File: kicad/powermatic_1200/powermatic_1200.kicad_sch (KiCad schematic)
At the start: 62 parts, among them J1 T4171310004-001, J2 3PH-4W-PLUG, J3 BNSPDX-23-W, J4 BSPDX-23-W, J5 BSPBX-22-W, K1 HMC-9B30-11-DS, K2 HMC-9B30-11-DS, K3 HC3096N-52-900-24, K4 HMC-9B30-11-DS, K5 HMC-9B30-11-DS, K6 HMC-9B30-11-DS, M1 PWRM1200-MOTOR, Q1 FAZ-D4/2-NA-L, SW1 222102

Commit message: massage schematic for understanding
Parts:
- removed J3: BNSPDX-23-W, Controls:BNSPDX-23-W_BottomWall, symbol Controls:BNSPDX-23-W
- removed J5: BSPBX-22-W, Controls:BSPBX-22-W_BottomWall, symbol Controls:BSPBX-22-W
- removed S2: 800 Type 3SA, symbol non_lcsc_parts:Non-LCSC/800S-3SA
- removed S3: 365-TAV2111, symbol non_lcsc_parts:Non-LCSC/365-TAV2111
- removed TB22, TB23: KN-T12GRY-25, Controls:KN-T12GRY-25_Front, symbol Controls:KN-T12GRY-25
- added J3: BSPBX-22-W, Controls:BSPBX-22-W_BottomWall, symbol non_lcsc_parts:Non-LCSC/BSPBX-22-W
- added J7: BNSPDX-23-W, Controls:BNSPDX-23-W_BottomWall, symbol Controls:BNSPDX-23-W
- added S2: 800 Type 3SA, symbol Controls:800S-3SA
- added S3: 365-TAV2111, symbol Controls:365-TAV2111
- added TB4, TB5, TB6, TB7, TB8: KN-T12GRY-25, Controls:KN-T12GRY-25_Front, symbol Controls:KN-T12GRY-25
- added TB53: KN-G12SP-10, Controls:KN-G12SP-10_Front, symbol Controls:KN-G12SP-10
- J2: Part Name Power Plug -> Mains Plug
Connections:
- net FWD_CMD: now also J3.5, S2.R1 (FWD_NO_2), TB6.BOT (TERM), TB6.TOP (TERM)
- net HIGH_CMD: now also J3.3, S3.2.U (HI2_U), TB5.BOT (TERM), TB5.TOP (TERM)
- net L1_IN: now also J7.X (L1)
- net L2_IN: now also J7.Y (L2)
- net L3_IN: now also J7.Z (L3)
- net LOW_CMD: now also J3.2, S3.1.U (LOW1_U), S3.3.U (HI3_U), TB4.BOT (TERM), TB4.TOP (TERM)
- net M1_T1: no longer TB61.BOT (TERM)
- net M1_T2: no longer TB63.BOT (TERM)
- net M1_T3: no longer TB65.BOT (TERM)
- net M1_T4: now also J4.T6, M1.T6, OL2.2 (T1), TB68.BOT (TERM), TB68.TOP (TERM); no longer J4.T4, M1.T4, OL2.4 (T2), TB66.BOT (TERM), TB66.TOP (TERM)
- net M1_T5: now also J4.T4, M1.T4, OL2.4 (T2), TB66.BOT (TERM), TB66.TOP (TERM); no longer J4.T5, M1.T5, OL2.6 (T3), TB67.BOT (TERM), TB67.TOP (TERM)
- net M1_T6: now also J4.T5, M1.T5, OL2.6 (T3), TB67.BOT (TERM), TB67.TOP (TERM); no longer J4.T6, M1.T6, OL2.2 (T1), TB68.BOT (TERM), TB68.TOP (TERM)
- net PE: now also J7.G (GND), TB53.BOT (TERM), TB53.PE, TB53.TOP (TERM)
- net REV_CMD: now also J3.6, S2.R3 (REV_NO_2), TB7.BOT (TERM), TB7.TOP (TERM)
- net ESTOP_JUMPER: now reaches J1.2, J1.3, J6.2, J6.3, S1.2 (NC2/WHI), S1.3 (NC1/BLK), TB31.BOT (TERM), TB31.TOP (TERM), TB32.BOT (TERM), TB32.TOP (TERM)
- net +24V_CTRL renamed STOP_RELEASED
- net STOP_RELEASED: now also J3.1, J3.7 (8), S2.L5 (STOP_NC_1), S3.1.L (LOW1_L), S3.2.L (HI2_L)
- net +24V_RUN renamed SPEED_SET
- net SPEED_SET: now also J3.4, S2.L2 (FWD_NO_1), S2.L4 (REV_NO_1)
- net STOP_CHAIN renamed OVERLOAD_OK
- net OVERLOAD_OK: now also J3.7 (8), S2.R5 (STOP_NC_2), TB8.BOT (TERM), TB8.TOP (TERM)
- new net: S3.3.L (HI3_L), S3.4.L (LOW4_L), S3.5.L (HI5_L)
- new net: S3.4.U (LOW4_U), S3.6.U (HI6_U)
- new net: S3.5.U (HI5_U), S3.7.U (LOW7_U)
- new net: S3.7.L (LOW7_L), S3.8.L (HI8_L)
- new net: S2.R2 (FWD_NC_2), S2.R4 (REV_NC_2)
- no-connect marks 20 -> 23
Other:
- note added: "DIN_BOT"
- note added: "DIN_TOP"
- note added: "J2.GND"
- note removed: "J2.G"
- note removed: "J5.1"
- note removed: "J5.2"
- note removed: "K1.43"
- note removed: "K2.43"
- note removed: "K4.43"
- note removed: "K4.44"
- note removed: "K5.2"
- note removed: "K5.4"
- note removed: "K5.6"
- note removed: "K6.43"
- note removed: "K6.44"
- note removed: "M1.T1"
- note removed: "M1.T2"
- note removed: "M1.T3"
- note removed: "M1.T4"
- note removed: "M1.T5"
- note removed: "M1.T6"
- note removed: "OL1A.2"
- note removed: "OL1A.4"
- note removed: "OL1A.6"
- note removed: "OL2A.2"
- note removed: "OL2A.4"
- note removed: "OL2A.6"
- note removed: "PS1.TB1.1"
- moved on the sheet: FH1, J1, J2, J4, J6, K1A, K2B, K4A, K4B, K5A, K5B, K6A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

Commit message: Integrate vintage controls and standardize panel artwork
Update the schematic, PCB, BOM and wiring-size/termination tools for the control-station and conduit plans. Preserve physical terminal mappings and detailed Fab artwork while reserving user layers for enclosure information. Include KiCad migration and review checkpoints; native DRC remains unverified after checker crashes.
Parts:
- removed J3: BSPBX-22-W, Controls:BSPBX-22-W_BottomWall, symbol non_lcsc_parts:Non-LCSC/BSPBX-22-W
- removed J4: BSPDX-23-W, Controls:BSPDX-23-W_BottomWall, symbol Controls:BSPDX-23-W
- removed J7: BNSPDX-23-W, Controls:BNSPDX-23-W_BottomWall, symbol Controls:BNSPDX-23-W
- removed K1, K2, K4, K5, K6: HMC-9B30-11-DS, Controls:HMC-9B30-11-DS_Front, symbol non_lcsc_parts:Non-LCSC/HMC-9B30-11-DS
- removed MI1, MI2: HMX1-MI, Controls:HMX1-MI_Front, symbol non_lcsc_parts:Non-LCSC/HMX1-MI
- removed OL1, OL2: HTOR32-6-S, Controls:HTOR32-6-S_Front, symbol non_lcsc_parts:Non-LCSC/HTOR32-6-S
- removed SP3: HMX1-SSVRC-DC, Controls:HMX1-SSVRC-DC_Front, symbol non_lcsc_parts:Non-LCSC/HMX1-SSVRC-DC
- removed TB1, TB10, TB11, TB12, TB13, TB14, TB2, TB20, TB21, TB24, TB3, TB30, TB31, TB32, TB33, TB4, TB40, TB41, TB42, TB5, TB6, TB60, TB61, TB62, TB63, TB64, TB65, TB66, TB67, TB68, TB7, TB8: KN-T12GRY-25, Controls:KN-T12GRY-25_Front, symbol Controls:KN-T12GRY-25
- removed TB50, TB51, TB52, TB53: KN-G12SP-10, Controls:KN-G12SP-10_Front, symbol Controls:KN-G12SP-10
- added K1, K2, K4, K5, K6: HMC-9B30-11-DS, Controls:HMC-9B30-11-DS_Front, symbol Controls:HMC-9B30-11-DS
- added OL4, OL6: HTOR32-6-S, Controls:HTOR32-6-S_Front, symbol Controls:HTOR32-6-S
- added SP6: HMX1-SSVRC-DC, Controls:HMX1-SSVRC-DC_Front, symbol non_lcsc_parts:Non-LCSC/HMX1-SSVRC-DC
- FH1: Mounting (none) -> din_top; Part Name Class R Fuse Holder -> Fuse Holder; Termination.P1.A (none) -> Ferrule 14 AWG; L=TBD mm; Termination.P1.B (none) -> Ferrule 14 AWG; L=TBD mm; Termination.P2.A (none) -> Ferrule 14 AWG; L=TBD mm; Termination.P2.B (none) -> Ferrule 14 AWG; L=TBD mm; Termination.P3.A (none) -> Ferrule 14 AWG; L=TBD mm; Termination.P3.B (none) -> Ferrule 14 AWG; L=TBD mm; Wire.Sizes (none) -> {"schema":1,"owner_uuid":"5ca8057b-4eb2-4c19-b9e6-24988ef26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; WireName Fuse Holder -> (none)
- H1: Mounting (none) -> panel; Termination.X1 (none) -> Ferrule 18 AWG; L=TBD mm; Termination.X2 (none) -> Ferrule 18 AWG; L=TBD mm; Wire.Sizes (none) -> {"schema":1,"owner_uuid":"a7bde42c-14f2-46ec-a0af-e6c2b915b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
- J1: Mounting (none) -> panel; Termination.1 (none) -> Factory pigtail, 22 AWG (retained); Termination.2 (none) -> Factory pigtail, 22 AWG (retained); Termination.3 (none) -> Factory pigtail, 22 AWG (retained); Termination.4 (none) -> Factory pigtail, 22 AWG (retained); Wire.Sizes (none) -> {"schema":1,"owner_uuid":"b4d1b4ae-f9ca-4a9a-a340-a64e26a69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
- J2: Mounting (none) -> machine; Termination.G (none) -> Plug clamp, 12 AWG; Termination.X (none) -> Plug clamp, 12 AWG; Termination.Y (none) -> Plug clamp, 12 AWG; Termination.Z (none) -> Plug clamp, 12 AWG; Wire.Sizes (none) -> {"schema":1,"owner_uuid":"c5ff8006-339f-4474-94f3-df6cc7c1d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; WireName Mains Plug -> (none)
- J6: value ~ -> (none); Mounting (none) -> machine; Termination.1 (none) -> M12 mating contact (retained); Termination.2 (none) -> M12 mating contact (retained); Termination.3 (none) -> M12 mating contact (retained); Termination.4 (none) -> M12 mating contact (retained); Wire.Sizes (none) -> {"schema":1,"owner_uuid":"b5200e46-0e22-4b8b-8db6-9eae3d708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
- K3: Mounting (none) -> din_bot; Termination.13 (none) -> Ferrule 18 AWG; L=TBD mm; Termination.14 (none) -> Ferrule 18 AWG; L=TBD mm; Termination.23 (none) -> Ferrule 18 AWG; L=TBD mm; Termination.24 (none) -> Ferrule 18 AWG; L=TBD mm; Termination.31 (none) -> N/A — unused pin; Termination.32 (none) -> N/A — unused pin; Termination.41 (none) -> N/A — unused pin; Termination.42 (none) -> N/A — unused pin; Termination.A1+ (none) -> Ferrule 18 AWG; L=TBD mm; Termination.A2 (none) -> Ferrule 18 AWG; L=TBD mm; Wire.Sizes (none) -> {"schema":1,"owner_uuid":"40692fa1-1db0-4fd6-bab3-8a72882b1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
- M1: Mounting (none) -> machine; Termination.PE (none) -> Wire-splice connector, 12 AWG; Termination.T1 (none) -> Wire-splice connector, 14 AWG; Termination.T2 (none) -> Wire-splice connector, 14 AWG; Termination.T3 (none) -> Wire-splice connector, 14 AWG; Termination.T4 (none) -> Wire-splice connector, 14 AWG; Termination.T5 (none) -> Wire-splice connector, 14 AWG; Termination.T6 (none) -> Wire-splice connector, 14 AWG; Wire.SizePlan (none) -> {"schema":1,"owner_uuid":"f758497e-4710-4fd6-9851-f0e206557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; Wire.Sizes (none) -> {"schema":1,"owner_uuid":"f758497e-4710-4fd6-9851-f0e206557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
- PS1: JLCPCB Assembly Unknown -> (none); JLCPCB Checked UTC 2026-09-23T00:57:12+00:00 -> (none); JLCPCB Class Unmapped -> (none); JLCPCB Match No exact MPN in returned results -> (none); JLCPCB Source https://jlcpcb.com/parts/componentSearch?searchTxt=NDR-240-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 -> (none); Mounting (none) -> din_bot; Termination.1_BOT (none) -> Ferrule 14 AWG; L=TBD mm; Termination.1_TOP (none) -> Ferrule 18 AWG; L=TBD mm; Termination.2_BOT (none) -> Ferrule 14 AWG; L=TBD mm; Termination.2_TOP (none) -> Ferrule 18 AWG; L=TBD mm; Termination.3_BOT (none) -> Ferrule 14 AWG; L=TBD mm; Termination.3_TOP (none) -> Ferrule 18 AWG; L=TBD mm; Termination.4_TOP (none) -> Ferrule 18 AWG; L=TBD mm; Wire.SizePlan (none) -> {"schema":1,"owner_uuid":"b71e1787-97a1-40f8-b061-785c34849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; Wire.Sizes (none) -> {"schema":1,"owner_uuid":"b71e1787-97a1-40f8-b061-785c34849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
- Q1: Mounting (none) -> din_bot; Termination.1 (none) -> Ferrule 14 AWG; L=TBD mm; Termination.2 (none) -> Ferrule 14 AWG; L=TBD mm; Termination.3 (none) -> Ferrule 14 AWG; L=TBD mm; Termination.4 (none) -> Ferrule 14 AWG; L=TBD mm; Wire.Sizes (none) -> {"schema":1,"owner_uuid":"b75c22a6-5008-468e-8688-fb1a0cea0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
- S1: Mounting (none) -> machine; Termination.1 (none) -> Supplied assembly connection (retained); Termination.2 (none) -> Supplied assembly connection (retained); Termination.3 (none) -> Supplied assembly connection (retained); Termination.4 (none) -> Supplied assembly connection (retained); Wire.Sizes (none) -> {"schema":1,"owner_uuid":"dbf6d1f8-0025-4137-ac1b-c2a9236e3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
- S2: value 800 Type 3SA -> 50MA3KLE; footprint (none) -> Controls:50MA3KLE_Top; symbol Controls:800S-3SA -> Controls:50MA3KLE; MPN (none) -> 50MA3KLE; Manufacturer Allen-Bradley -> Furnas; Mounting (none) -> machine; Package (none) -> Machine-mounted pushbutton station 52 x 116 x 44.7 mm; Termination.1B (none) -> Ring terminal, 16 AWG; stud=#8-32; OD<=9 mm; Termination.1T (none) -> Retained jumper; Termination.2B (none) -> Ring terminal, 16 AWG; stud=#8-32; OD<=9 mm; Termination.2T (none) -> N/A — unused pin; Termination.3B (none) -> Ring terminal, 16 AWG; stud=#8-32; OD<=9 mm; Termination.3T (none) -> Retained jumper; Termination.4B (none) -> Required jumper, 2B-4B; Termination.4T (none) -> N/A — unused pin; Termination.5T (none) -> Ring terminal, 16 AWG; stud=#8-32; OD<=9 mm; Termination.6T (none) -> Ring terminal, 16 AWG; stud=#8-32; OD<=9 mm; Wire.Sizes (none) -> {"schema":1,"owner_uuid":"9cff5cf5-fbfa-495e-9dc5-ac2f98a5c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
- S3: footprint (none) -> Controls:365-TAV2111_Top; Mounting (none) -> machine; Package (none) -> Machine-mounted drum switch 156 x 73 x 75 mm; Termination.1.L (none) -> Ring terminal, 16 AWG; stud=#8-32; OD<=9 mm; Termination.1.U (none) -> Ring terminal, 16 AWG; stud=#8-32; OD<=9 mm; Termination.2.L (none) -> Retained jumper; Termination.2.U (none) -> Ring terminal, 16 AWG; stud=#8-32; OD<=9 mm; Termination.3.L (none) -> Retained jumper; Termination.3.U (none) -> Retained jumper; Termination.4.L (none) -> Retained jumper; Termination.4.U (none) -> Retained jumper; Termination.5.L (none) -> Retained jumper; Termination.5.U (none) -> Retained jumper; Termination.6.L (none) -> N/A — unused pin; Termination.6.U (none) -> Retained jumper; Termination.7.L (none) -> Retained jumper; Termination.7.U (none) -> Retained jumper; Termination.8.L (none) -> Retained jumper; Termination.8.U (none) -> N/A — unused pin; Wire.Sizes (none) -> {"schema":1,"owner_uuid":"26502bde-0b19-4cea-bdff-2e8d228f3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
- SP1: Mounting (none) -> din_top; Termination.1 (none) -> Supplied fork-ended lead (retained); Termination.2 (none) -> Supplied fork-ended lead (retained); Wire.Sizes (none) -> {"schema":1,"owner_uuid":"c89c0a24-66e3-4ec6-9e05-4125689b4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
- SP2: Mounting (none) -> din_top; Termination.1 (none) -> Supplied fork-ended lead (retained); Termination.2 (none) -> Supplied fork-ended lead (retained); Wire.Sizes (none) -> {"schema":1,"owner_uuid":"cf360c79-7593-4c8a-bc81-2460b3d4c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
- SP4: Mounting (none) -> din_bot; Termination.1 (none) -> Supplied fork-ended lead (retained); Termination.2 (none) -> Supplied fork-ended lead (retained); Wire.Sizes (none) -> {"schema":1,"owner_uuid":"243d7eb4-7102-4a9f-94c3-46f62fdca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
- SP5: Mounting (none) -> din_bot; Termination.1 (none) -> Supplied fork-ended lead (retained); Termination.2 (none) -> Supplied fork-ended lead (retained); Wire.Sizes (none) -> {"schema":1,"owner_uuid":"8ee9f0e8-f022-4223-9694-e57327052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
- SW1: Mounting (none) -> panel; Termination.1 (none) -> Ferrule 14 AWG; L=TBD mm; Termination.2 (none) -> Ferrule 14 AWG; L=TBD mm; Termination.3 (none) -> Ferrule 14 AWG; L=TBD mm; Termination.4 (none) -> Ferrule 14 AWG; L=TBD mm; Termination.5 (none) -> Ferrule 14 AWG; L=TBD mm; Termination.6 (none) -> Ferrule 14 AWG; L=TBD mm; Wire.Sizes (none) -> {"schema":1,"owner_uuid":"de43fc54-ea53-4062-9d14-222047b23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
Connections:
- net +24V_EN: now also OL4.95 (TRIP_NC_1)
- net 0V: now also K1.A2.BOT (A2_BOT), K1.A2.TOP (A2_TOP), K2.A2.BOT (A2_BOT), K2.A2.TOP (A2_TOP), K4.A2.BOT (A2_BOT), K4.A2.TOP (A2_TOP), K5.A2.BOT (A2_BOT), K5.A2.TOP (A2_TOP), K6.A2.BOT (A2_BOT), K6.A2.TOP (A2_TOP), SP6.2 (SUP_2)
- net FWD_CMD: now also S2.1B (FWD_NO_1), K1.44 (AUX_NO_2), K2.31 (AUX_NC_1); no longer S2.R1 (FWD_NO_2)
- net HIGH_CMD: now also K4.31 (AUX_NC_1)
- net HS_SHORT: now also K5.1 (L1), K5.3 (L2), K5.5 (L3)
- net L1_DIR: now also K1.2 (T1), K2.6 (T3), K4.1 (L1), K6.1 (L1)
- net L1_SW: now also K1.1 (L1), K2.1 (L1)
- net L2_DIR: now also K1.4 (T2), K2.4 (T2), K4.3 (L2), K6.3 (L2)
- net L2_SW: now also K1.3 (L2), K2.3 (L2)
- net L3_DIR: now also K1.6 (T3), K2.2 (T1), K4.5 (L3), K6.5 (L3)
- net L3_SW: now also K1.5 (L3), K2.5 (L3)
- net LOW_CMD: now also K6.31 (AUX_NC_1)
- net M1_T1: now also K5.2 (T1), OL4.2 (T1)
- net M1_T2: now also K5.4 (T2), OL4.4 (T2)
- net M1_T3: now also K5.6 (T3), OL4.6 (T3)
- net M1_T4: now also M1.T4, OL6.2 (T1); no longer M1.T6
- net M1_T5: now also M1.T5, OL6.4 (T2); no longer M1.T4
- net M1_T6: now also M1.T6, OL6.6 (T3); no longer M1.T5
- net OVERLOAD_OK: now also S2.1T (FWD_NC_1), S2.3T (REV_NC_1), S2.5T (STOP_NC_1), OL6.96 (TRIP_NC_2); no longer S2.R5 (STOP_NC_2)
- net PE: now also M1.PE
- net REV_CMD: now also S2.3B (REV_NO_1), K1.31 (AUX_NC_1), K2.44 (AUX_NO_2); no longer S2.R3 (REV_NO_2)
- net SPEED_SET: now also S2.2B (FWD_NO_2), S2.4B (REV_NO_2), K1.43 (AUX_NO_1), K2.43 (AUX_NO_1), K4.44 (AUX_NO_2), K6.44 (AUX_NO_2); no longer S2.L2 (FWD_NO_1), S2.L4 (REV_NO_1)
- net STOP_RELEASED: now also S2.6T (STOP_NC_2), K4.43 (AUX_NO_1), K6.43 (AUX_NO_1); no longer S2.L5 (STOP_NC_1)
- net HS_COIL: now reaches SP5.1 (SUP_1)
- net HS_COIL: now also K4.32 (AUX_NC_2), K5.43 (AUX_NO_1), K5.A1.BOT (A1_BOT), K5.A1.TOP (A1_TOP)
- net FWD_COIL: now reaches SP1.1 (SUP_1)
- net FWD_COIL: now also K1.A1.BOT (A1_BOT), K1.A1.TOP (A1_TOP), K2.32 (AUX_NC_2)
- net REV_COIL: now reaches SP2.1 (SUP_1)
- net REV_COIL: now also K1.32 (AUX_NC_2), K2.A1.BOT (A1_BOT), K2.A1.TOP (A1_TOP)
- net K3_JUMPER: now reaches K3.14 (NO1), K3.23 (NO2)
- net LOW_COIL: now reaches SP4.1 (SUP_1)
- net LOW_COIL: now also K4.A1.BOT (A1_BOT), K4.A1.TOP (A1_TOP), K5.32 (AUX_NC_2)
- new net HIGH_COIL: K5.44 (AUX_NO_2), K6.A1.BOT (A1_BOT), K6.A1.TOP (A1_TOP), SP6.1 (SUP_1)
- new net L1_HIGH: K6.2 (T1), OL6.IN1 (L1)
- new net L1_LOW: K4.2 (T1), OL4.IN1 (L1)
- new net L2_HIGH: K6.4 (T2), OL6.IN2 (L2)
- new net L2_LOW: K4.4 (T2), OL4.IN2 (L2)
- new net L3_HIGH: K6.6 (T3), OL6.IN3 (L3)
- new net L3_LOW: K4.6 (T3), OL4.IN3 (L3)
- new net LOW_K6_OK: K5.31 (AUX_NC_1), K6.32 (AUX_NC_2)
- new net OL4_OK: OL4.96 (TRIP_NC_2), OL6.95 (TRIP_NC_1)
- no-connect marks 23 -> 12
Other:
- note removed: "3"
- note removed: "4"
- note removed: "5"
- note removed: "BACKPLATE"
- note removed: "DIN_BOT"
- note removed: "DIN_TOP"
- note removed: "DOOR"
- note removed: "H1.X1"
- note removed: "H1.X2"
- note removed: "J1.1"
- note removed: "J2.GND"
- note removed: "K1.A2_BOT"
- note removed: "K2.A2_BOT"
- note removed: "K3.13"
- note removed: "K3.A2"
- note removed: "K4.A2_BOT"
- note removed: "K5.A2_BOT"
- note removed: "K6.A2_BOT"
- note removed: "MOTOR"
- note removed: "PS1.TB2.1"
- note removed: "PS1.TB2.3"
- note removed: "SPARE"
- moved on the sheet: FH1, H1, J1, J2, J6, K3, PS1, Q1, S1, S2, S3, SW1

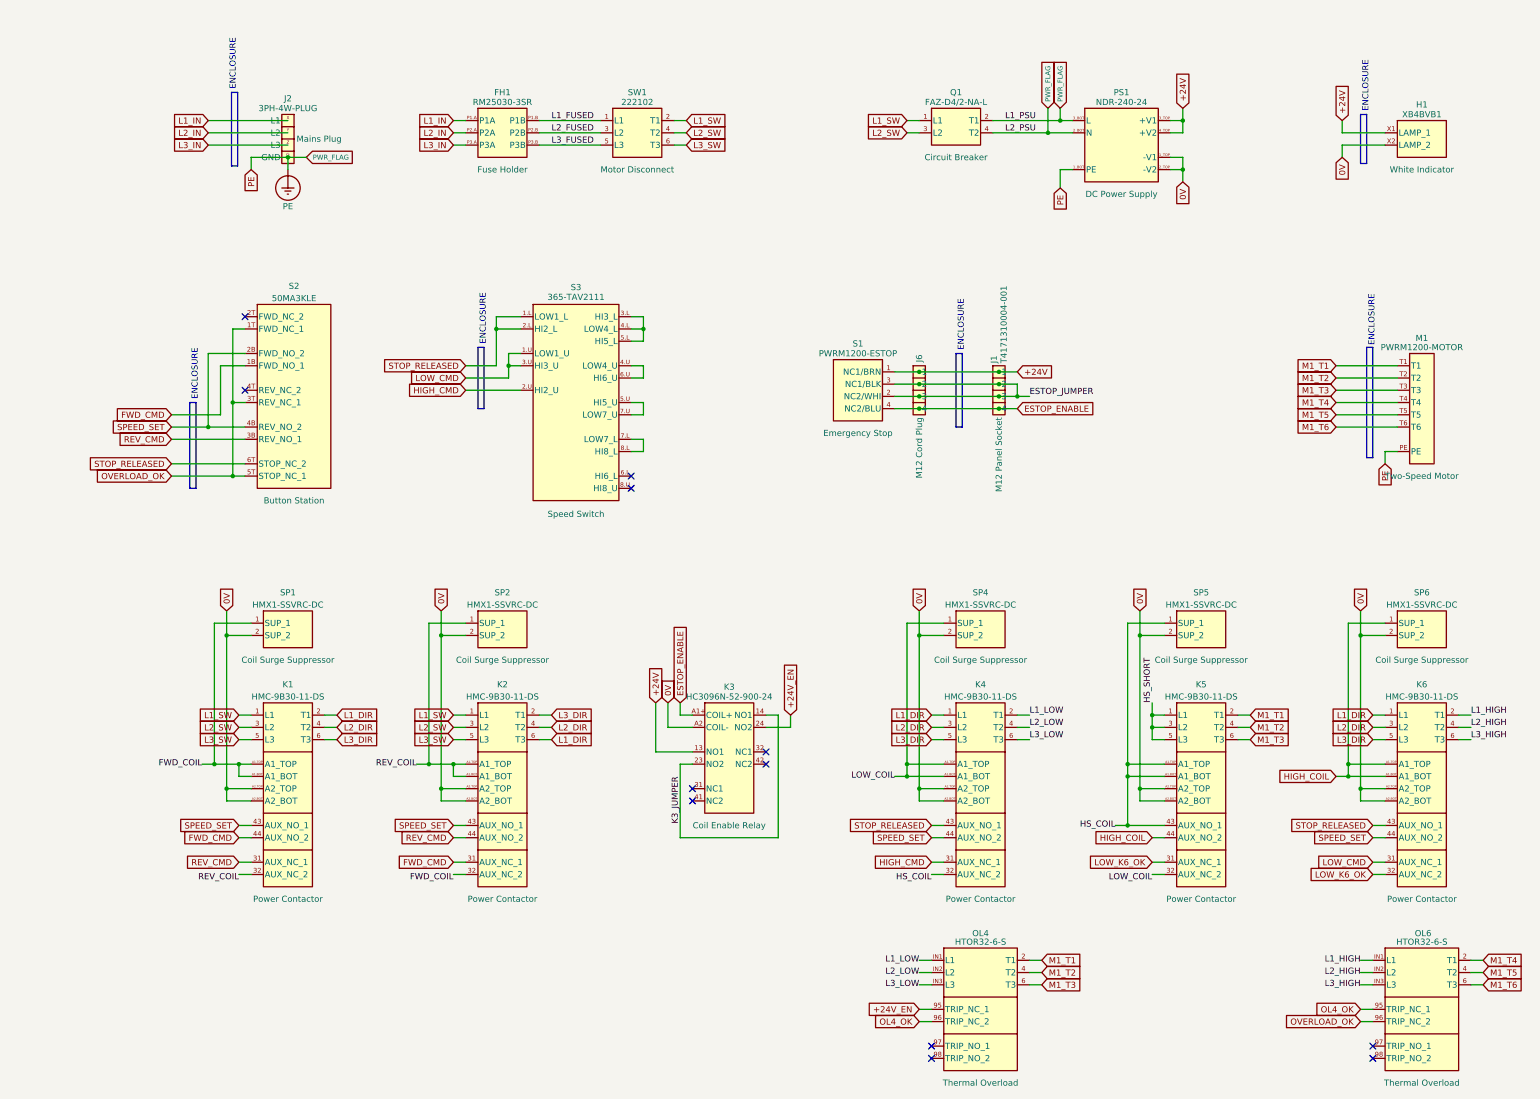
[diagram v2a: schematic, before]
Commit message: Update panel wiring metadata and KiCad schedule extraction
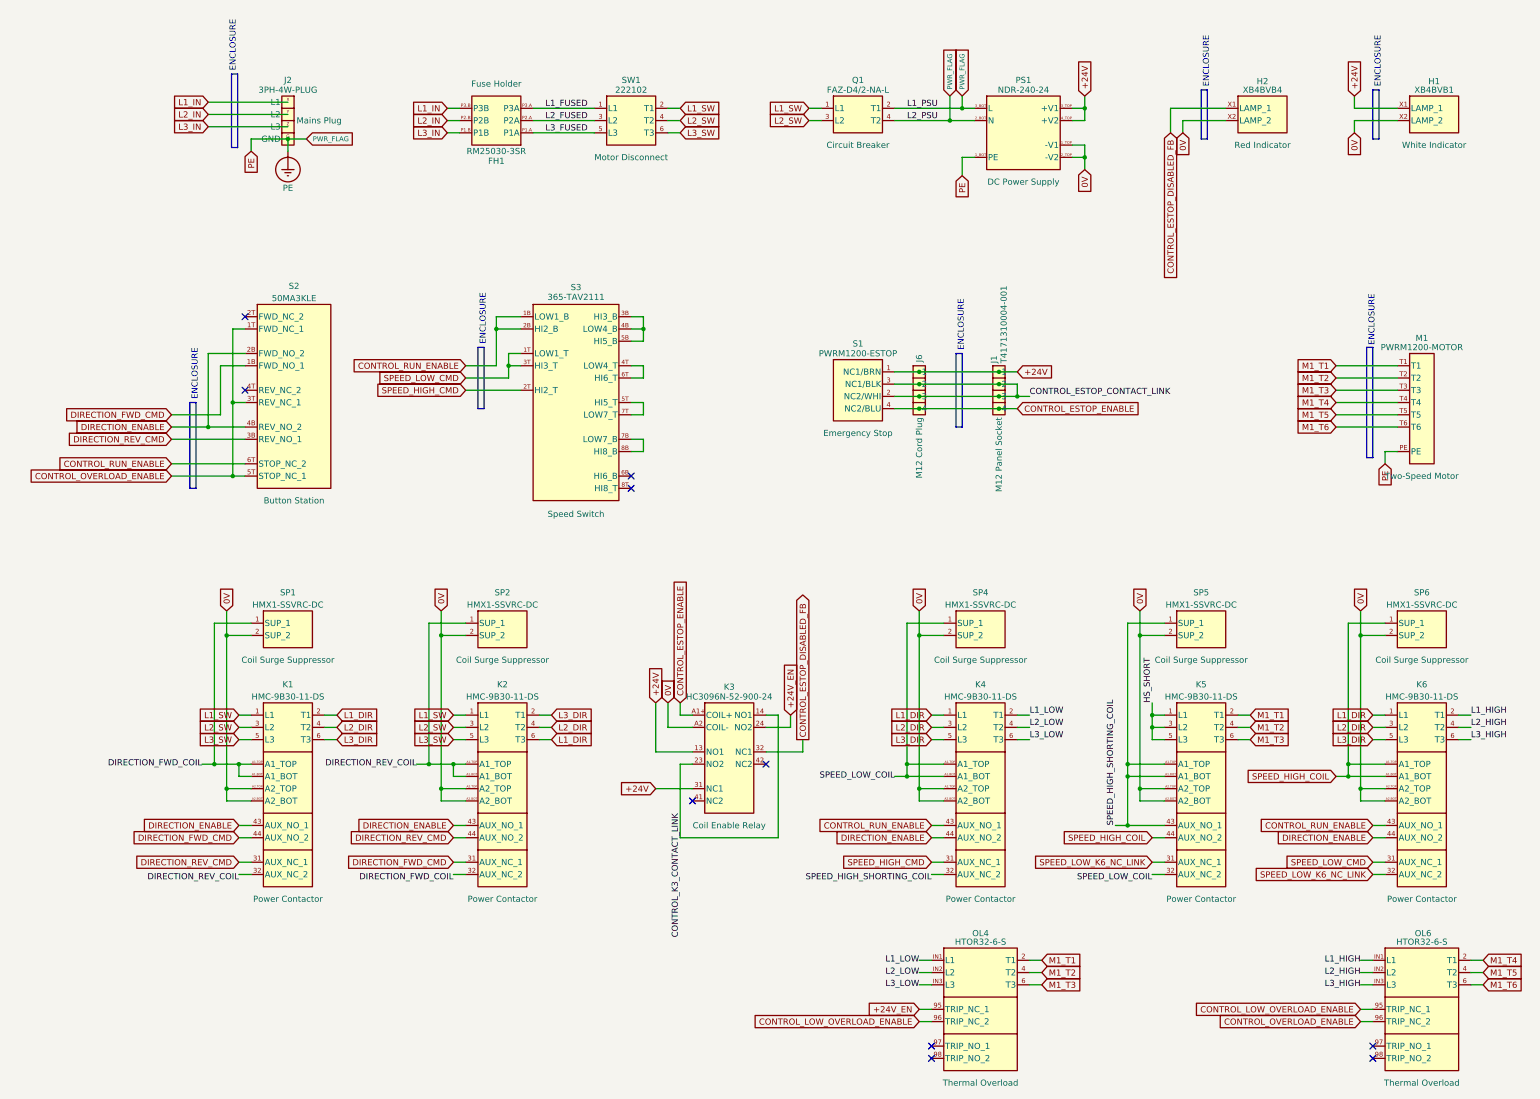
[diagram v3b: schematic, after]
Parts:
- removed H1: XB4BVB1, Controls:XB4BVB1_LeftWall, symbol Controls:XB4BVB1
- added H1: XB4BVB1, Controls:XB4BVB1_LeftWall, symbol non_lcsc_parts:Non-LCSC/XB4BVB1
- added H2: XB4BVB4, Controls:XB4BVB4_LeftWall, symbol non_lcsc_parts:Non-LCSC/XB4BVB4
- FH1: Termination.P1.A Ferrule 14 AWG; L=TBD mm -> (none); Termination.P1.B Ferrule 14 AWG; L=TBD mm -> (none); Termination.P2.A Ferrule 14 AWG; L=TBD mm -> (none); Termination.P2.B Ferrule 14 AWG; L=TBD mm -> (none); Termination.P3.A Ferrule 14 AWG; L=TBD mm -> (none); Termination.P3.B Ferrule 14 AWG; L=TBD mm -> (none); Wire.Sizes {"schema":1,"owner_uuid":"5ca8057b-4eb2-4c19-b9e6-24988ef269e0","entries":[{"pin":"P1.A","net":"L1_IN","scope":"panel_power","awg":14,"color":"Black"},{"pin":"P1.B","net":"/L1_FUSED","scope":"panel_power","awg":14,"color":"Black"},{"pin":"P2.A","net":"L2_IN","scope":"panel_power","awg":14,"color":"Black"},{"pin":"P2.B","net":"/L2_FUSED","scope":"panel_power","awg":14,"color":"Black"},{"pin":"P3.A","net":"L3_IN","scope":"panel_power","awg":14,"color":"Black"},{"pin":"P3.B","net":"/L3_FUSED","scope":"panel_power","awg":14,"color":"Black"}]} -> {"schema":1,"owner_uuid":"5ca8057b-4eb2-4c19-b9e6-24988ef269e0","entries":[{"pin":"P1.A","net":"/L3_FUSED","scope":"panel_power","awg":14,"color":"Black"},{"pin":"P1.B","net":"L3_IN","scope":"panel_power","awg":14,"color":"Black"},{"pin":"P2.A","net":"/L2_FUSED","scope":"panel_power","awg":14,"color":"Black"},{"pin":"P2.B","net":"L2_IN","scope":"panel_power","awg":14,"color":"Black"},{"pin":"P3.A","net":"/L1_FUSED","scope":"panel_power","awg":14,"color":"Black"},{"pin":"P3.B","net":"L1_IN","scope":"panel_power","awg":14,"color":"Black"}]}
- J1: Termination.1 Factory pigtail, 22 AWG (retained) -> (none); Termination.2 Factory pigtail, 22 AWG (retained) -> (none); Termination.3 Factory pigtail, 22 AWG (retained) -> (none); Termination.4 Factory pigtail, 22 AWG (retained) -> (none); Wire.Sizes {"schema":1,"owner_uuid":"b4d1b4ae-f9ca-4a9a-a340-a64e26a697f9","entries":[{"pin":"1","net":"+24V","scope":"factory_pigtail","awg":22,"color":"Brown","note":"T4171310004-001 factory 0.34 mm² / 22 AWG lead; any extension is a separate wire."},{"pin":"2","net":"/ESTOP_JUMPER","scope":"factory_pigtail","awg":22,"color":"White","note":"T4171310004-001 factory 0.34 mm² / 22 AWG lead; any extension is a separate wire."},{"pin":"3","net":"/ESTOP_JUMPER","scope":"factory_pigtail","awg":22,"color":"Blue","note":"T4171310004-001 factory 0.34 mm² / 22 AWG lead; any extension is a separate wire."},{"pin":"4","net":"ESTOP_ENABLE","scope":"factory_pigtail","awg":22,"color":"Black","note":"T4171310004-001 factory 0.34 mm² / 22 AWG lead; any extension is a separate wire."}]} -> {"schema":1,"owner_uuid":"b4d1b4ae-f9ca-4a9a-a340-a64e26a697f9","entries":[{"pin":"1","net":"+24V","scope":"factory_pigtail","awg":22,"color":"Brown","note":"T4171310004-001 factory 0.34 mm² / 22 AWG lead; any extension is a separate wire."},{"pin":"2","net":"/CONTROL_ESTOP_CONTACT_LINK","scope":"factory_pigtail","awg":22,"color":"White","note":"T4171310004-001 factory 0.34 mm² / 22 AWG lead; any extension is a separate wire."},{"pin":"3","net":"/CONTROL_ESTOP_CONTACT_LINK","scope":"factory_pigtail","awg":22,"color":"Blue","note":"T4171310004-001 factory 0.34 mm² / 22 AWG lead; any extension is a separate wire."},{"pin":"4","net":"CONTROL_ESTOP_ENABLE","scope":"factory_pigtail","awg":22,"color":"Black","note":"T4171310004-001 factory 0.34 mm² / 22 AWG lead; any extension is a separate wire."}]}
- J2: footprint (none) -> Controls:BNSPDX-23-W_MainsPlug_BottomWall; Termination.G Plug clamp, 12 AWG -> (none); Termination.X Plug clamp, 12 AWG -> (none); Termination.Y Plug clamp, 12 AWG -> (none); Termination.Z Plug clamp, 12 AWG -> (none); Wire.W001 {"schema":1,"from_pin":"X","to":{"symbol_uuid":"782cabbe-a58e-46f3-9f97-d5cf96f2f77e","pin":"BOT"},"section":"01 Incoming phases","kind":"panel_cable_core","review":"pending","awg":"12","term1":"plug clamp","term2":"Ferrule 12 AWG; L=TBD mm","length":{"mode":"auto","slack_mm":"200","round_mm":"50","minimum_mm":"400"},"migration_note":"The legacy cut estimate is retained as a minimum until this section is reviewed. Length covers the panel tail; external cable allowance remains in the BOM.","route_from":{"symbol_uuid":"233d10ed-562b-4d7c-8332-858e4146f140","pin":"X"},"from_symbol_uuid":"c5ff8006-339f-4474-94f3-df6cc7c1d5be"} -> {"schema":1,"from_pin":"X","to":{"symbol_uuid":"782cabbe-a58e-46f3-9f97-d5cf96f2f77e","pin":"BOT"},"section":"01 Incoming phases","kind":"panel_cable_core","review":"pending","awg":"12","length":{"mode":"auto","slack_mm":"200","round_mm":"50","minimum_mm":"400"},"migration_note":"The legacy cut estimate is retained as a minimum until this section is reviewed. Length covers the panel tail; external cable allowance remains in the BOM.","route_from":{"symbol_uuid":"233d10ed-562b-4d7c-8332-858e4146f140","pin":"X"},"from_symbol_uuid":"c5ff8006-339f-4474-94f3-df6cc7c1d5be"}; Wire.W003 {"schema":1,"from_pin":"Y","to":{"symbol_uuid":"28685e83-b92d-43bf-876f-d867e00acc25","pin":"BOT"},"section":"01 Incoming phases","kind":"panel_cable_core","review":"pending","awg":"12","term1":"plug clamp","term2":"Ferrule 12 AWG; L=TBD mm","length":{"mode":"auto","slack_mm":"200","round_mm":"50","minimum_mm":"400"},"migration_note":"The legacy cut estimate is retained as a minimum until this section is reviewed. Length covers the panel tail; external cable allowance remains in the BOM.","route_from":{"symbol_uuid":"233d10ed-562b-4d7c-8332-858e4146f140","pin":"Y"},"from_symbol_uuid":"c5ff8006-339f-4474-94f3-df6cc7c1d5be"} -> {"schema":1,"from_pin":"Y","to":{"symbol_uuid":"28685e83-b92d-43bf-876f-d867e00acc25","pin":"BOT"},"section":"01 Incoming phases","kind":"panel_cable_core","review":"pending","awg":"12","length":{"mode":"auto","slack_mm":"200","round_mm":"50","minimum_mm":"400"},"migration_note":"The legacy cut estimate is retained as a minimum until this section is reviewed. Length covers the panel tail; external cable allowance remains in the BOM.","route_from":{"symbol_uuid":"233d10ed-562b-4d7c-8332-858e4146f140","pin":"Y"},"from_symbol_uuid":"c5ff8006-339f-4474-94f3-df6cc7c1d5be"}; Wire.W005 {"schema":1,"from_pin":"Z","to":{"symbol_uuid":"d4d821a2-498b-4b0e-b253-9376599824db","pin":"BOT"},"section":"01 Incoming phases","kind":"panel_cable_core","review":"pending","awg":"12","term1":"plug clamp","term2":"Ferrule 12 AWG; L=TBD mm","length":{"mode":"auto","slack_mm":"200","round_mm":"50","minimum_mm":"400"},"migration_note":"The legacy cut estimate is retained as a minimum until this section is reviewed. Length covers the panel tail; external cable allowance remains in the BOM.","route_from":{"symbol_uuid":"233d10ed-562b-4d7c-8332-858e4146f140","pin":"Z"},"from_symbol_uuid":"c5ff8006-339f-4474-94f3-df6cc7c1d5be"} -> {"schema":1,"from_pin":"Z","to":{"symbol_uuid":"d4d821a2-498b-4b0e-b253-9376599824db","pin":"BOT"},"section":"01 Incoming phases","kind":"panel_cable_core","review":"pending","awg":"12","length":{"mode":"auto","slack_mm":"200","round_mm":"50","minimum_mm":"400"},"migration_note":"The legacy cut estimate is retained as a minimum until this section is reviewed. Length covers the panel tail; external cable allowance remains in the BOM.","route_from":{"symbol_uuid":"233d10ed-562b-4d7c-8332-858e4146f140","pin":"Z"},"from_symbol_uuid":"c5ff8006-339f-4474-94f3-df6cc7c1d5be"}
- J6: Termination.1 M12 mating contact (retained) -> (none); Termination.2 M12 mating contact (retained) -> (none); Termination.3 M12 mating contact (retained) -> (none); Termination.4 M12 mating contact (retained) -> (none); Wire.Sizes {"schema":1,"owner_uuid":"b5200e46-0e22-4b8b-8db6-9eae3d708854","entries":[{"pin":"1","net":"+24V","scope":"connector_interface","awg":null,"note":"M12 mating interface; retain the supplied assembly."},{"pin":"2","net":"/ESTOP_JUMPER","scope":"connector_interface","awg":null,"note":"M12 mating interface; retain the supplied assembly."},{"pin":"3","net":"/ESTOP_JUMPER","scope":"connector_interface","awg":null,"note":"M12 mating interface; retain the supplied assembly."},{"pin":"4","net":"ESTOP_ENABLE","scope":"connector_interface","awg":null,"note":"M12 mating interface; retain the supplied assembly."}]} -> {"schema":1,"owner_uuid":"b5200e46-0e22-4b8b-8db6-9eae3d708854","entries":[{"pin":"1","net":"+24V","scope":"connector_interface","awg":null,"note":"M12 mating interface; retain the supplied assembly."},{"pin":"2","net":"/CONTROL_ESTOP_CONTACT_LINK","scope":"connector_interface","awg":null,"note":"M12 mating interface; retain the supplied assembly."},{"pin":"3","net":"/CONTROL_ESTOP_CONTACT_LINK","scope":"connector_interface","awg":null,"note":"M12 mating interface; retain the supplied assembly."},{"pin":"4","net":"CONTROL_ESTOP_ENABLE","scope":"connector_interface","awg":null,"note":"M12 mating interface; retain the supplied assembly."}]}
- K1: Termination.1 Ferrule 14 AWG; L=TBD mm -> (none); Termination.2 Ferrule 14 AWG; L=TBD mm -> (none); Termination.3 Ferrule 14 AWG; L=TBD mm -> (none); Termination.31 Ferrule 18 AWG; L=TBD mm -> (none); Termination.32 Ferrule 18 AWG; L=TBD mm -> (none); Termination.4 Ferrule 14 AWG; L=TBD mm -> (none); Termination.43 Ferrule 18 AWG; L=TBD mm -> (none); Termination.44 Twin ferrule 2 × 18 AWG; L=TBD mm -> (none); Termination.5 Ferrule 14 AWG; L=TBD mm -> (none); Termination.6 Ferrule 14 AWG; L=TBD mm -> (none); Termination.A1.BOT Ferrule 18 AWG; L=TBD mm -> (none); Termination.A1.TOP Ferrule 18 AWG; L=TBD mm -> (none); Termination.A2.BOT Ferrule 18 AWG; L=TBD mm -> (none); Termination.A2.TOP Ferrule 18 AWG; L=TBD mm -> (none); Wire.Sizes {"schema":1,"owner_uuid":"d223283d-de9b-4327-854a-5af43f940011","entries":[{"pin":"1","net":"L1_SW","scope":"panel_power","awg":14,"color":"Black","note":"Gauge for discrete panel wire; reversing connection-kit bars retain their supplied form."},{"pin":"2","net":"L1_DIR","scope":"panel_power","awg":14,"color":"Black","note":"Gauge for discrete panel wire; reversing connection-kit bars retain their supplied form."},{"pin":"3","net":"L2_SW","scope":"panel_power","awg":14,"color":"Black","note":"Gauge for discrete panel wire; reversing connection-kit bars retain their supplied form."},{"pin":"31","net":"REV_CMD","scope":"panel_control","awg":18,"color":"Blue"},{"pin":"32","net":"/REV_COIL","scope":"panel_control","awg":18,"color":"Blue"},{"pin":"4","net":"L2_DIR","scope":"panel_power","awg":14,"color":"Black","note":"Gauge for discrete panel wire; reversing connection-kit bars retain their supplied form."},{"pin":"43","net":"SPEED_SET","scope":"panel_control","awg":18,"color":"Blue"},{"p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 -> {"schema":1,"owner_uuid":"d223283d-de9b-4327-854a-5af43f940011","entries":[{"pin":"1","net":"L1_SW","scope":"panel_power","awg":14,"color":"Black","note":"Gauge for discrete panel wire; reversing connection-kit bars retain their supplied form."},{"pin":"2","net":"L1_DIR","scope":"panel_power","awg":14,"color":"Black","note":"Gauge for discrete panel wire; reversing connection-kit bars retain their supplied form."},{"pin":"3","net":"L2_SW","scope":"panel_power","awg":14,"color":"Black","note":"Gauge for discrete panel wire; reversing connection-kit bars retain their supplied form."},{"pin":"31","net":"DIRECTION_REV_CMD","scope":"panel_control","awg":18,"color":"Blue"},{"pin":"32","net":"/DIRECTION_REV_COIL","scope":"panel_control","awg":18,"color":"Blue"},{"pin":"4","net":"L2_DIR","scope":"panel_power","awg":14,"color":"Black","note":"Gauge for discrete panel wire; reversing connection-kit bars retain their supplied form."},{"pin":"43","net":"DIRECTION_ENABLE","scope":"panel_control","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
- K2: Termination.1 Ferrule 14 AWG; L=TBD mm -> (none); Termination.2 Ferrule 14 AWG; L=TBD mm -> (none); Termination.3 Ferrule 14 AWG; L=TBD mm -> (none); Termination.31 Ferrule 18 AWG; L=TBD mm -> (none); Termination.32 Ferrule 18 AWG; L=TBD mm -> (none); Termination.4 Ferrule 14 AWG; L=TBD mm -> (none); Termination.43 Ferrule 18 AWG; L=TBD mm -> (none); Termination.44 Twin ferrule 2 × 18 AWG; L=TBD mm -> (none); Termination.5 Ferrule 14 AWG; L=TBD mm -> (none); Termination.6 Ferrule 14 AWG; L=TBD mm -> (none); Termination.A1.BOT Ferrule 18 AWG; L=TBD mm -> (none); Termination.A1.TOP Ferrule 18 AWG; L=TBD mm -> (none); Termination.A2.BOT Ferrule 18 AWG; L=TBD mm -> (none); Termination.A2.TOP Ferrule 18 AWG; L=TBD mm -> (none); Wire.Sizes {"schema":1,"owner_uuid":"e654422b-9a6f-4ebb-86fa-0867c299ae4a","entries":[{"pin":"1","net":"L1_SW","scope":"panel_power","awg":14,"color":"Black","note":"Gauge for discrete panel wire; reversing connection-kit bars retain their supplied form."},{"pin":"2","net":"L3_DIR","scope":"panel_power","awg":14,"color":"Black","note":"Gauge for discrete panel wire; reversing connection-kit bars retain their supplied form."},{"pin":"3","net":"L2_SW","scope":"panel_power","awg":14,"color":"Black","note":"Gauge for discrete panel wire; reversing connection-kit bars retain their supplied form."},{"pin":"31","net":"FWD_CMD","scope":"panel_control","awg":18,"color":"Blue"},{"pin":"32","net":"/FWD_COIL","scope":"panel_control","awg":18,"color":"Blue"},{"pin":"4","net":"L2_DIR","scope":"panel_power","awg":14,"color":"Black","note":"Gauge for discrete panel wire; reversing connection-kit bars retain their supplied form."},{"pin":"43","net":"SPEED_SET","scope":"panel_control","awg":18,"color":"Blue"},{"p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 -> {"schema":1,"owner_uuid":"e654422b-9a6f-4ebb-86fa-0867c299ae4a","entries":[{"pin":"1","net":"L1_SW","scope":"panel_power","awg":14,"color":"Black","note":"Gauge for discrete panel wire; reversing connection-kit bars retain their supplied form."},{"pin":"2","net":"L3_DIR","scope":"panel_power","awg":14,"color":"Black","note":"Gauge for discrete panel wire; reversing connection-kit bars retain their supplied form."},{"pin":"3","net":"L2_SW","scope":"panel_power","awg":14,"color":"Black","note":"Gauge for discrete panel wire; reversing connection-kit bars retain their supplied form."},{"pin":"31","net":"DIRECTION_FWD_CMD","scope":"panel_control","awg":18,"color":"Blue"},{"pin":"32","net":"/DIRECTION_FWD_COIL","scope":"panel_control","awg":18,"color":"Blue"},{"pin":"4","net":"L2_DIR","scope":"panel_power","awg":14,"color":"Black","note":"Gauge for discrete panel wire; reversing connection-kit bars retain their supplied form."},{"pin":"43","net":"DIRECTION_ENABLE","scope":"panel_control","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
- K3: Termination.13 Ferrule 18 AWG; L=TBD mm -> (none); Termination.14 Ferrule 18 AWG; L=TBD mm -> (none); Termination.23 Ferrule 18 AWG; L=TBD mm -> (none); Termination.24 Ferrule 18 AWG; L=TBD mm -> (none); Termination.31 N/A — unused pin -> (none); Termination.32 N/A — unused pin -> (none); Termination.41 N/A — unused pin -> (none); Termination.42 N/A — unused pin -> (none); Termination.A1+ Ferrule 18 AWG; L=TBD mm -> (none); Termination.A2 Ferrule 18 AWG; L=TBD mm -> (none); Wire.Sizes {"schema":1,"owner_uuid":"40692fa1-1db0-4fd6-bab3-8a72882b147f","entries":[{"pin":"13","net":"+24V","scope":"panel_control","awg":18,"color":"Blue"},{"pin":"14","net":"/K3_JUMPER","scope":"panel_control","awg":18,"color":"Blue"},{"pin":"23","net":"/K3_JUMPER","scope":"panel_control","awg":18,"color":"Blue"},{"pin":"24","net":"+24V_EN","scope":"panel_control","awg":18,"color":"Blue"},{"pin":"A1+","net":"ESTOP_ENABLE","scope":"panel_control","awg":18,"color":"Blue"},{"pin":"A2","net":"0V","scope":"panel_control","awg":18,"color":"Blue"}]} -> {"schema":1,"owner_uuid":"40692fa1-1db0-4fd6-bab3-8a72882b147f","entries":[{"pin":"13","net":"+24V","scope":"panel_control","awg":18,"color":"Blue"},{"pin":"14","net":"/CONTROL_K3_CONTACT_LINK","scope":"panel_control","awg":18,"color":"Blue"},{"pin":"23","net":"/CONTROL_K3_CONTACT_LINK","scope":"panel_control","awg":18,"color":"Blue"},{"pin":"24","net":"+24V_EN","scope":"panel_control","awg":18,"color":"Blue"},{"pin":"A1+","net":"CONTROL_ESTOP_ENABLE","scope":"panel_control","awg":18,"color":"Blue"},{"pin":"A2","net":"0V","scope":"panel_control","awg":18,"color":"Blue"},{"pin":"31","net":"+24V","scope":"panel_control","awg":18,"color":"Blue"},{"pin":"32","net":"CONTROL_ESTOP_DISABLED_FB","scope":"panel_control","awg":18,"color":"Blue"}]}
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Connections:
- net +24V: now also K3.31 (NC1), H1.X1 (LAMP_1)
- net 0V: now also H1.X2 (LAMP_2), H2.X2 (LAMP_2)
- net L1_FUSED: now also FH1.P3.A (P3A); no longer FH1.P1.B (P1B)
- net L1_IN: now also FH1.P3.B (P3B); no longer FH1.P1.A (P1A)
- net L2_FUSED: now also FH1.P2.A (P2A); no longer FH1.P2.B (P2B)
- net L2_IN: now also FH1.P2.B (P2B); no longer FH1.P2.A (P2A)
- net L3_FUSED: now also FH1.P1.A (P1A); no longer FH1.P3.B (P3B)
- net L3_IN: now also FH1.P1.B (P1B); no longer FH1.P3.A (P3A)
- net CONTROL_ESTOP_DISABLED_FB: now reaches K3.32 (NC1)
- net CONTROL_ESTOP_DISABLED_FB: now also H2.X1 (LAMP_1)
- net ESTOP_ENABLE renamed CONTROL_ESTOP_ENABLE
- net ESTOP_JUMPER renamed CONTROL_ESTOP_CONTACT_LINK
- net FWD_CMD renamed DIRECTION_FWD_CMD
- net FWD_COIL renamed DIRECTION_FWD_COIL
- net HIGH_CMD renamed SPEED_HIGH_CMD
- net SPEED_HIGH_CMD: now also S3.2T (HI2_T); no longer S3.2.U (HI2_U)
- net HIGH_COIL renamed SPEED_HIGH_COIL
- net HS_COIL renamed SPEED_HIGH_SHORTING_COIL
- net K3_JUMPER renamed CONTROL_K3_CONTACT_LINK
- removed net LOW_CMD: K6.31 (AUX_NC_1), S3.1.U (LOW1_U), S3.3.U (HI3_U)
- net LOW_COIL renamed SPEED_LOW_COIL
- net LOW_K6_OK renamed SPEED_LOW_K6_NC_LINK
- net OL4_OK renamed CONTROL_LOW_OVERLOAD_ENABLE
- net OVERLOAD_OK renamed CONTROL_OVERLOAD_ENABLE
- net REV_CMD renamed DIRECTION_REV_CMD
- net REV_COIL renamed DIRECTION_REV_COIL
- net SPEED_SET renamed DIRECTION_ENABLE
- net STOP_RELEASED renamed CONTROL_RUN_ENABLE
- net CONTROL_RUN_ENABLE: now also S3.1B (LOW1_B), S3.2B (HI2_B); no longer S3.1.L (LOW1_L), S3.2.L (HI2_L)
- new net: S3.3B (HI3_B), S3.4B (LOW4_B), S3.5B (HI5_B)
- new net: S3.4T (LOW4_T), S3.6T (HI6_T)
- new net: S3.5T (HI5_T), S3.7T (LOW7_T)
- new net: S3.7B (LOW7_B), S3.8B (HI8_B)
- new net SPEED_LOW_CMD: K6.31 (AUX_NC_1), S3.1T (LOW1_T), S3.3T (HI3_T)
- no-connect marks 12 -> 10
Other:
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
